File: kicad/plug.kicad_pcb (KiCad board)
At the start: 2 copper layers, 11 parts, among them J1 74320-1004, P1 HDMI_RECEPTACLE

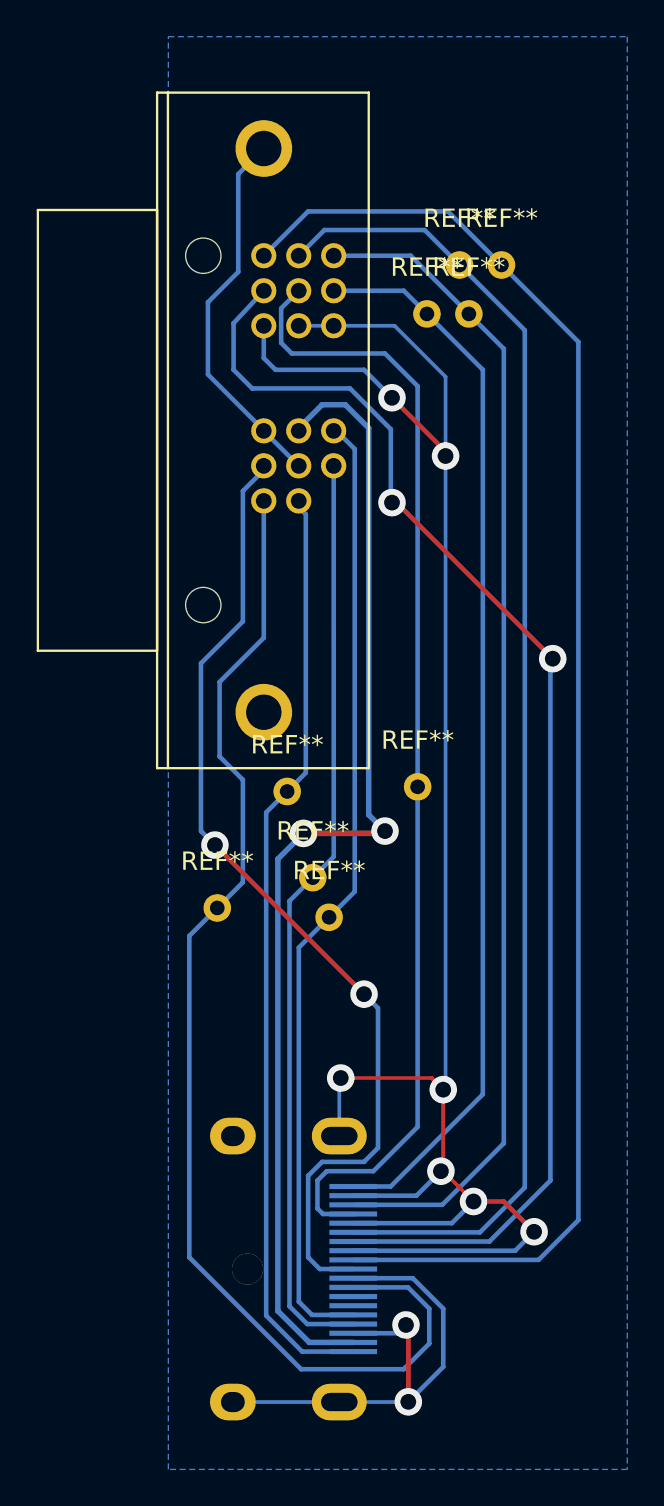
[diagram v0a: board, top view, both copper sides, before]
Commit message: reduced pcb height
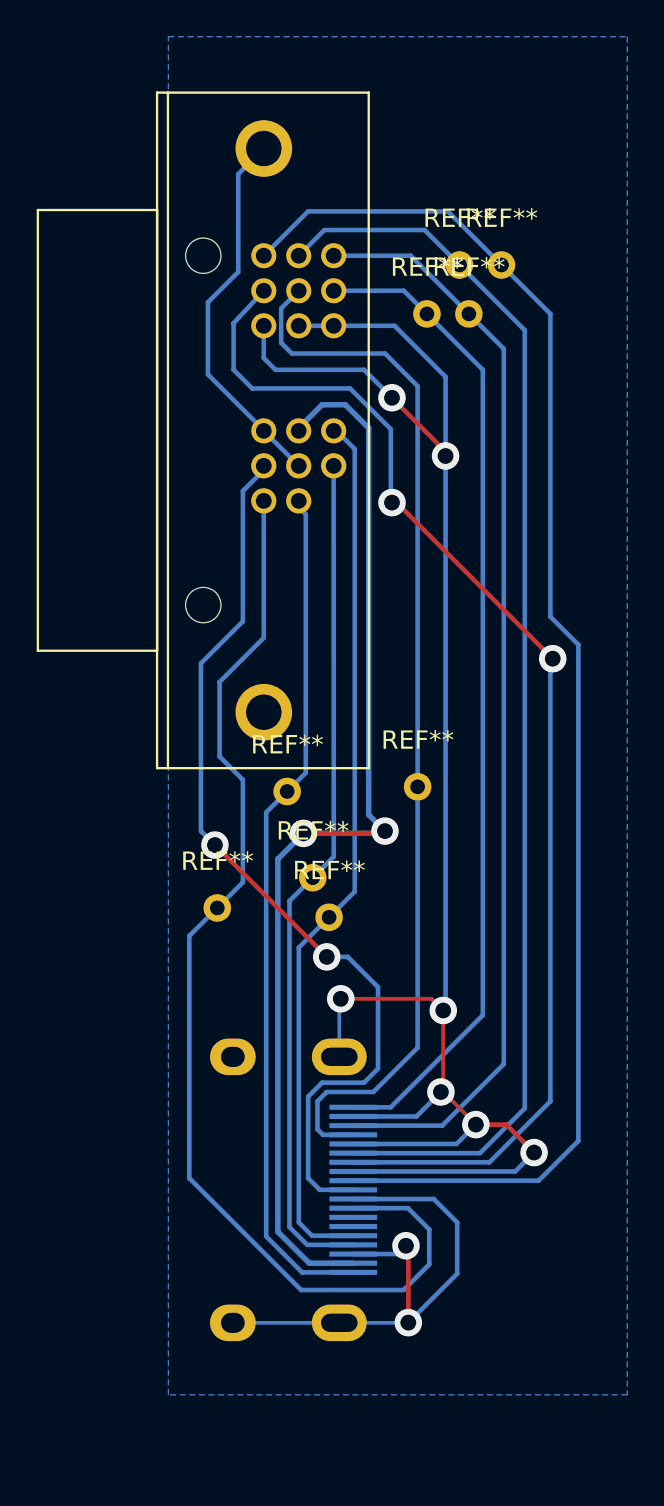
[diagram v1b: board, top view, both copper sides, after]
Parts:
- moved P1 4.32 mm to (90.7, 103.6)
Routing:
- net /hotplug: track 51.3 -> 46.8 mm
- net /D2-: track 64.2 -> 59.8 mm
- net /D0-: track 82.1 -> 77.8 mm
- net /CL-: track 66.6 -> 62.2 mm
- net /DDCdata: track 50.8 -> 46.5 mm
- net /DDCcl: track 52.7 -> 48.4 mm
- net /D2+: track 58.6 -> 54.2 mm
- net /D1-: track 72.3 -> 67.9 mm
- net /D1+: track 62.4 -> 58.1 mm
- net /+5v: track 63.3 -> 59.0 mm
- net /D0+: track 71.8 -> 67.7 mm
- net /CL+: track 55.5 -> 51.9 mm
- net /GND: track 153.7 -> 151.0 mm
